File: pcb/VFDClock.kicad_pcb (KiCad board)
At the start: 4 copper layers, 80 x 52.7 mm, 84 parts, among them J1 Conn_01x04_Socket, J2 L_SIG_CONN, J3 L_PWR_CONN, J4 USB_C_Receptacle_USB2.0_16P, J5 R_SIG_CONN, J6 R_PWR_CONN, J7 Conn_02x06_Top_Bottom, Q1 BSS138, SW1 SW_SPST, SW2 SW_SPST, SW3 SW_SPST, SW4 SW_SPST, SW5 SW_SPST, SW6 SW_SPST, U1 TBD62783AFWG, U10 AMS1117-1.5, U2 ESP32-S3-WROOM-1, U3 IP4234CZ6, U4 TBD62783AFNG, U5 SN74HC595PWR, U6 AMS1117-3.3, U7 DS3231MZ+TRL, U8 SHT45-AD1B-R2, U9 VEML3235SL

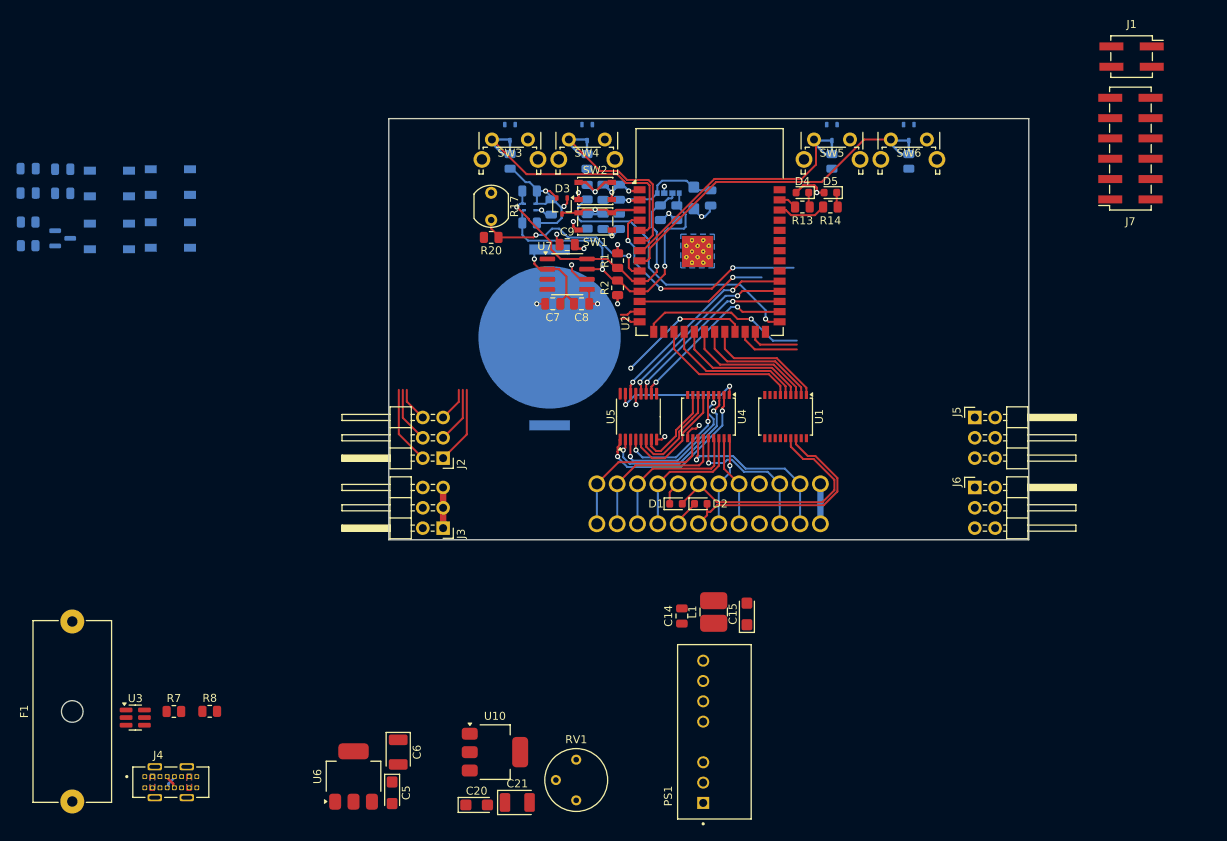
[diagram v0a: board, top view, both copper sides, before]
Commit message: Footprint placement done, PWR needs connecting
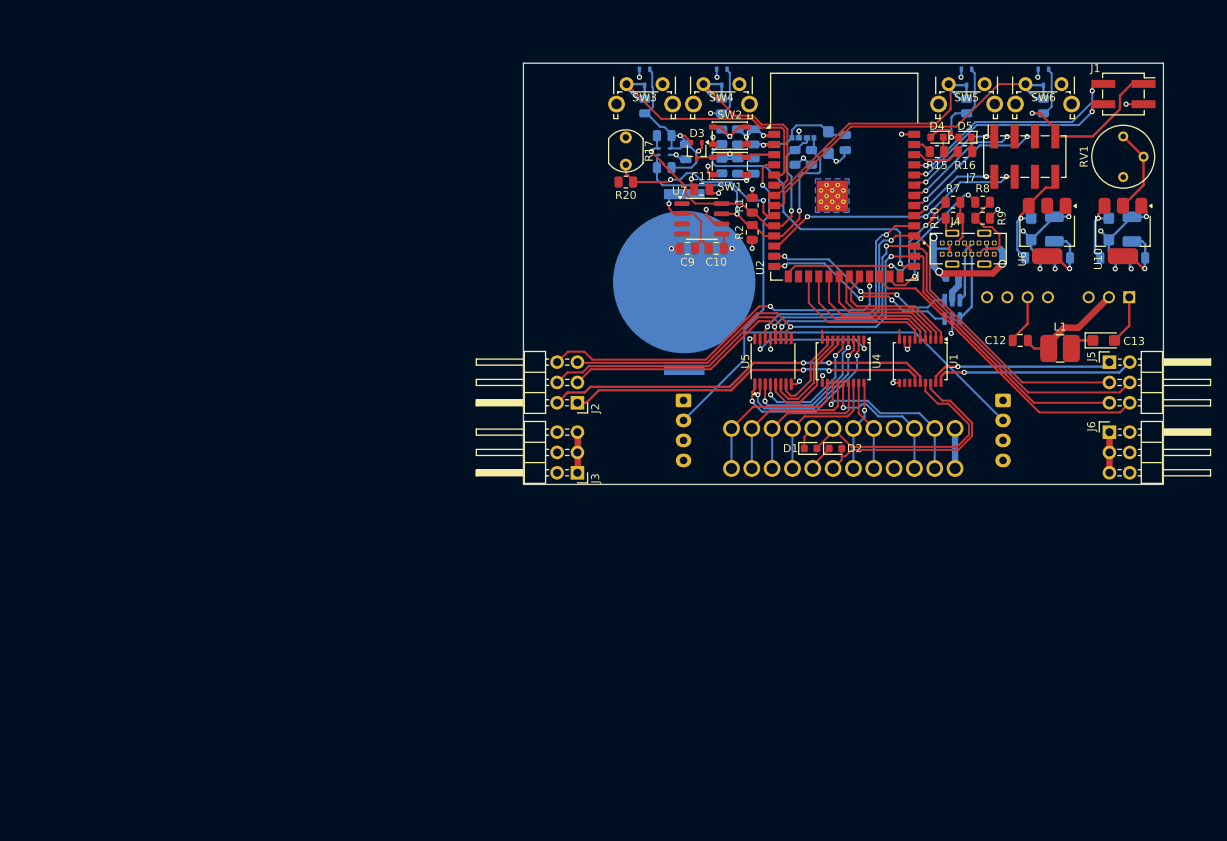
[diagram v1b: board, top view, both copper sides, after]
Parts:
- removed the C10 at (46.9, 95.7)
- removed the C11 at (46.9, 92.6)
- removed the C12 at (51.2, 95.7)
- removed the C13 at (51.2, 92.7)
- removed D10, D11: Inolux_IN-PI554FCH, LED_SMD:LED_Inolux_IN-PI554FCH_PLCC4_5.0x5.0mm_P3.2mm
- removed the D8 at (57.1, 101.1)
- removed the D9 at (57.1, 94.5)
- removed Q1: BSS138, Package_TO_SOT_SMD:SOT-23
- removed the R15 at (46.9, 102.2)
- removed the R16 at (46.9, 99.3)
- added C17: 100n, Capacitor_SMD:C_0805_2012Metric, B.Cu at (181.9, 103.8)
- added C20: 100n, Capacitor_SMD:C_0805_2012Metric, B.Cu at (185.6, 103.8)
- added C5: 100n, Capacitor_SMD:C_0805_2012Metric, B.Cu at (172.5, 103.8)
- added C8: 100n, Capacitor_SMD:C_0805_2012Metric, B.Cu at (176.2, 103.8)
- added J8: L_COL_CONN, Connector_JST:JST_XH_B4B-XH-A_1x04_P2.50mm_Vertical, B.Cu at (128.8, 121.6)
- added J9: R_COL_CONN, Connector_JST:JST_XH_B4B-XH-A_1x04_P2.50mm_Vertical, B.Cu at (168.8, 121.6)
- added R7: 100k, Resistor_SMD:R_0805_2012Metric, F.Cu at (162.5, 96.8)
- added R8: 100k, Resistor_SMD:R_0805_2012Metric, F.Cu at (166.2, 96.8)
- C18: renamed from C20; moved to B.Cu
- C19: renamed from C21; moved to B.Cu
- C6: renamed from C5; moved to B.Cu
- C7: renamed from C6; moved to B.Cu
- F1: value 3,5 A -> 2,5 A Fast Blow; footprint Fuse:Fuseholder_Cylinder-5x20mm_Schurter_0031_8201_Horizontal_Open -> Fuse:Fuse_0603_1608Metric; moved to B.Cu
- J7: value Conn_02x06_Top_Bottom -> CONN_GPIO; footprint Connector_PinSocket_2.54mm:PinSocket_2x06_P2.54mm_Vertical_SMD -> Connector_PinSocket_2.54mm:PinSocket_2x04_P2.54mm_Vertical_SMD
- PS1, U3: moved to B.Cu
- moved F1 128.0 mm to (162.4, 106.3), turned to 0 degrees
- moved J4 119.9 mm to (164.4, 102.6)
- moved R10 115.3 mm to (162.5, 98.8)
- moved R9 114.6 mm to (166.2, 98.8), turned to 180 degrees
- moved U3 114.2 mm to (162.4, 110.2), turned to 90 degrees
- moved U6 110.3 mm to (174.3, 100.4), turned to -90 degrees
- moved RV1 107.5 mm to (183.8, 88.6), turned to 180 degrees
- moved C18 106.9 mm to (182.0, 100.2), turned to -90 degrees
- moved C6 106.5 mm to (172.3, 100.2)
- moved C19 105.1 mm to (184.9, 100.2), turned to 90 degrees
- moved C7 104.9 mm to (175.2, 100.2), turned to 90 degrees
- moved U10 102.0 mm to (183.8, 100.4), turned to -90 degrees
- moved PS1 68.2 mm to (175.7, 110.1), turned to 180 degrees
- moved C13 56.2 mm to (181.4, 114.1), turned to 0 degrees
- moved C12 54.5 mm to (170.9, 114.1), turned to 180 degrees
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- renumbered C8 to C10, C9 to C11, C14 to C12, C15 to C13, C16 to C14, C17 to C15, C18 to C16, C7 to C9, D12 to D8, D13 to D9, R7 to R10, R9 to R11, R10 to R12, R11 to R13, R12 to R14, R13 to R15, R14 to R16, R8 to R9
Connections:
- F1 pad 1: +5V -> Net-(F1-Pad1)
- F1 pad 2: Net-(U3-VP) -> +5V
- J1 pad 3: Net-(J1-Pin_3) -> GND
- J1 pad 4: GND -> Net-(J1-Pin_4)
- J2 pad 2: /SRCLK -> /GRID_L2
- J2 pad 3: /GRID_L2 -> /RCLK
- J2 pad 4: //SRCLR -> /SRCLK
- J2 pad 5: /SER_LEFT -> //SRCLR
- J2 pad 6: /RCLK -> /SER_LEFT
- J4 pad A4: +5V -> Net-(F1-Pad1)
- J4 pad A9: +5V -> Net-(F1-Pad1)
- J4 pad B4: +5V -> Net-(F1-Pad1)
- J4 pad B9: +5V -> Net-(F1-Pad1)
- J5 pad 2: /SRCLK -> /GRID_R2
- J5 pad 3: /GRID_R2 -> /RCLK
- J5 pad 4: //SRCLR -> /SRCLK
- J5 pad 5: /SER_RIGHT -> //SRCLR
- J5 pad 6: /RCLK -> /SER_RIGHT
- J7 pad 1: +3V3 -> /GPIO42
- J7 pad 2: +5V -> /GPIO39
- J7 pad 3: /GPIO3 -> /GPIO41
- J7 pad 4: /GPIO41 -> /GPIO8
- J7 pad 5: /GPIO8 -> /GPIO40
- J7 pad 6: /GPIO42 -> GND
- J7 pad 7: /GPIO39 -> +3V3
- J7 pad 8: /GPIO48 -> +5V
- R10 pad 1: Net-(J4-CC1) -> GND
- R10 pad 2: GND -> Net-(J4-CC1)
- R9 pad 1: Net-(J4-CC2) -> GND
- R9 pad 2: GND -> Net-(J4-CC2)
- U2 pad 36: Net-(J1-Pin_3) -> Net-(J1-Pin_4)
- U3 pad 5: Net-(U3-VP) -> +5V
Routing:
- net /SRCLK: track 32.1 -> 96.7 mm
- net /RCLK: track 28.0 -> 91.7 mm
- net //SRCLR: track 28.3 -> 89.3 mm
- net +3V3: track 50.4 -> 111.2 mm, vias 8 -> 12
- net GND: track 37.2 -> 91.7 mm, vias 15 -> 33
- net /COLON_LED: track 29.1 -> 74.8 mm, vias 3 -> 1
- net /GRID_L2: track 7.02 -> 48.9 mm, vias 0 -> 2
- net /GRID_L1: track 9.77 -> 45.1 mm, vias 0 -> 2
- net +5V: track 5.08 -> 39.3 mm, vias 0 -> 2
- net /SER_RIGHT: track 7.95 -> 39.0 mm
- net Net-(J1-Pin_2): track 0.00 -> 29.2 mm, vias 0 -> 2
- net Net-(J1-Pin_4): track 0.00 -> 27.8 mm, vias 0 -> 2
- net /SER_LEFT: track 21.0 -> 46.7 mm
- net /GRID_R2: track 0.00 -> 25.1 mm, vias 0 -> 1
- net Net-(F1-Pad1): track 0.00 -> 24.2 mm, vias 0 -> 3
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- removed copper zone on B.Cu, net +5V
- removed copper zone on F.Cu, net +5V

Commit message: Layout done, generated fabrication files
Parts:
- added H1: MountingHole_Pad, MountingHole:MountingHole_3.2mm_M3_ISO14580_Pad_TopBottom, F.Cu at (112.2, 83.0)
- added H2: MountingHole_Pad, MountingHole:MountingHole_3.2mm_M3_ISO14580_Pad_TopBottom, F.Cu at (122.0, 128.0)
- added H3: MountingHole_Pad, MountingHole:MountingHole_3.2mm_M3_ISO14580_Pad_TopBottom, F.Cu at (176.0, 128.0)
- C1: value 22u -> 10u; footprint Capacitor_SMD:C_0805_2012Metric -> Capacitor_Tantalum_SMD:CP_EIA-3216-18_Kemet-A
- J2: value L_SIG_CONN -> R_SIG_CONN
- J5: value R_SIG_CONN -> L_SIG_CONN
- moved J8 39.9 mm to (168.8, 121.6)
- moved J9 39.9 mm to (128.8, 121.6)
- moved L1 2.98 mm to (175.9, 112.1)
- moved C13 2.59 mm to (179.7, 112.1), turned to -90 degrees
- moved C12 2.35 mm to (172.2, 112.1), turned to 90 degrees
- moved C1 0.63 mm to (135.6, 88.0)
- moved D3 0.18 mm to (130.3, 90.4)
- moved R12 0.08 mm to (133.5, 88.6)
- moved BT1 0.08 mm to (128.9, 106.7)
- moved C2 0.07 mm to (137.7, 88.6)
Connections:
- J2 pad 6: /SER_LEFT -> /SER_RIGHT
- J5 pad 6: /SER_RIGHT -> /SER_LEFT
- U2 pad 23: /SER_LEFT -> /SER_RIGHT
- U2 pad 24: /SER_RIGHT -> /SER_LEFT
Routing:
- net +3V3: track 111.2 -> 263.9 mm, vias 12 -> 14
- net +5V: track 39.3 -> 161.2 mm, vias 2 -> 8
- net Vfilament: track 5.00 -> 45.9 mm
- net Vbat: track 13.6 -> 43.0 mm, vias 1 -> 2
- net Vanode: track 8.54 -> 31.5 mm, vias 0 -> 2
- net Net-(F1-Pad1): track 24.2 -> 32.8 mm, vias 3 -> 2
- net /SER_RIGHT: track 39.0 -> 46.8 mm, vias 0 -> 2
- net /SER_LEFT: track 46.7 -> 39.0 mm, vias 2 -> 0
- net +1V5: track 19.0 -> 25.3 mm
- net GND: track 91.7 -> 95.1 mm, vias 33 -> 113
- net /SDA: track 41.5 -> 40.8 mm
- net Net-(U4-I1): track 16.5 -> 17.0 mm
- net /GPIO8: vias 3 -> 2
- added copper zone on B.Cu, net +5V
- added copper zone on In2.Cu, net +5V
- added copper zone on F.Cu, net Vanode
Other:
- board text added: "BOOT"
- board text added: "BTN1"
- board text added: "BTN2"
- board text added: "BTN3"
- board text added: "BTN4"
- board text added: "CR2032"
- board text added: "Filament ADJ"
- board text added: "L Module"
- board text added: "PWR"
- board text added: "R Module"
- board text added: "RST"
- board text added: "UART"

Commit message: Readded light sensor 3D model
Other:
- board text added: "PCB3D_BR_main"
- board text added: "PCB3D_TL_main"
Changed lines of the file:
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@@
 		)
 		(embedded_fonts no)
+		(model "${KIPRJMOD}/Models/VEML3235SL.stp"
+			(offset
+				(xyz 0 0.9 0.75)
+			)
+			(scale
+				(xyz 1 1 1)
+			)
+			(rotate
+				(xyz -90 -0 -0)
+			)
+		)
 	)
 	(footprint "Connector_PinSocket_2.54mm:PinSocket_1x12_P2.54mm_Vertical"
@@
 		)
 	)
+	(gr_text "PCB3D_TL_main"
+		(at 107.2 77.9 0)
+		(layer "Dwgs.User")
+		(effects
+			(font
+				(size 1 1)
+				(thickness 0.15)
+			)
+			(justify left bottom)
+		)
+	)
+	(gr_text "PCB3D_BR_main"
+		(at 190.8 134.6 0)
+		(layer "Dwgs.User")
+		(effects
+			(font
+				(size 1 1)
+				(thickness 0.15)
+			)
+			(justify left bottom)
+		)
+	)

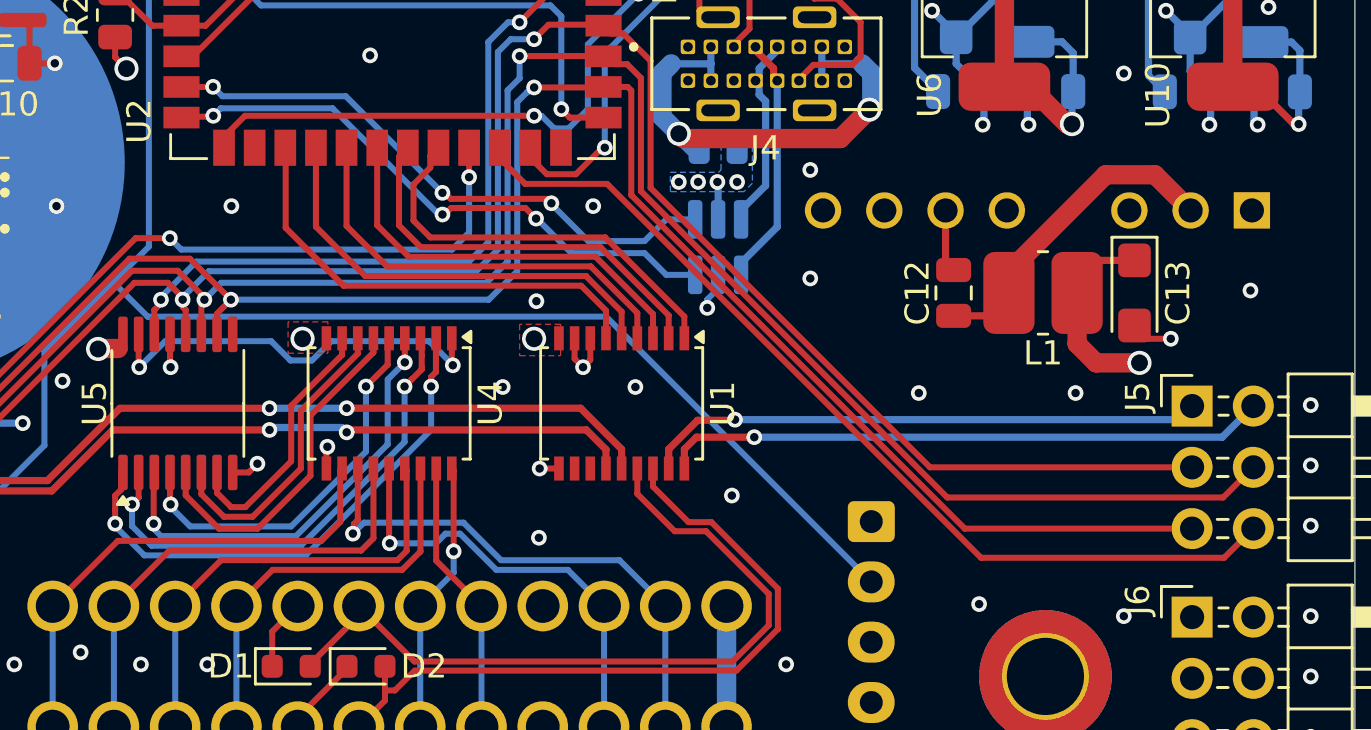
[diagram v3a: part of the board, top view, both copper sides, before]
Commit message: Modified circuit to use synchronous grid clock on all modules
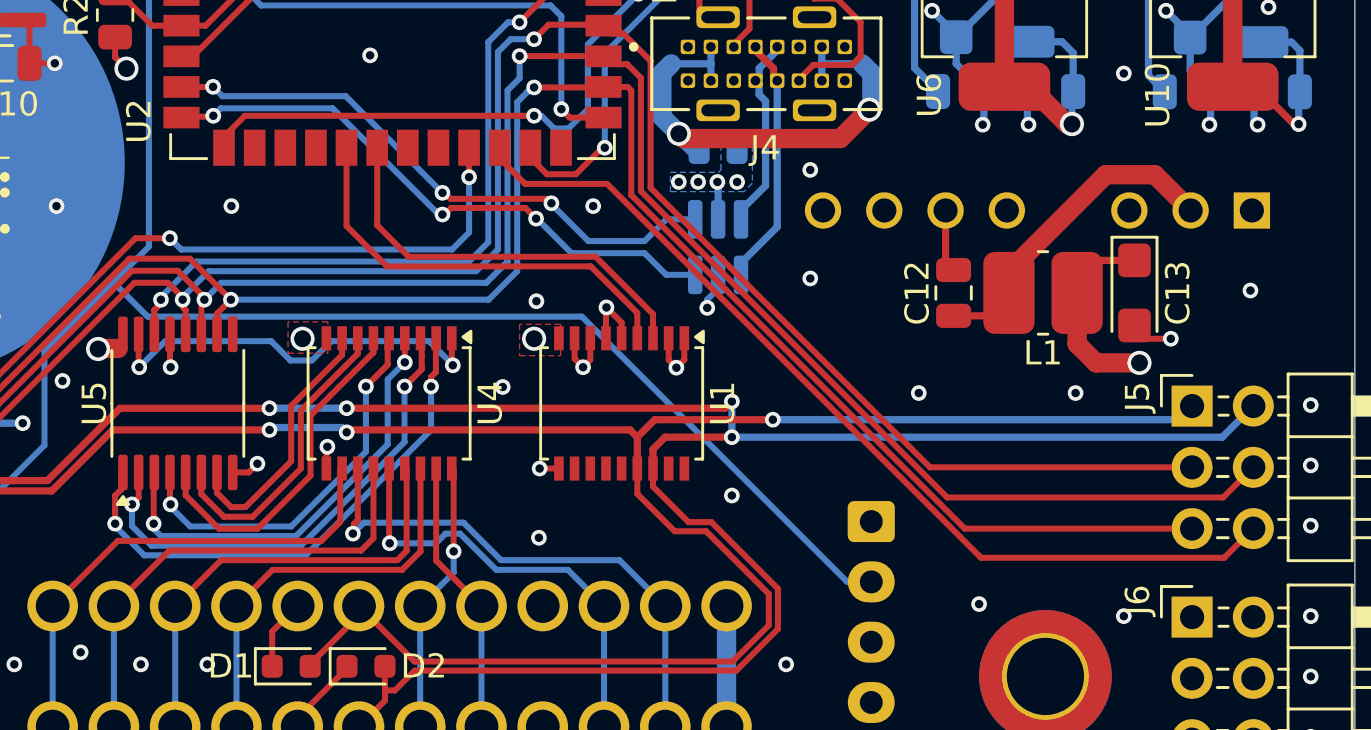
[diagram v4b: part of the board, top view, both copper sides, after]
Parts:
- J3: value L_PWR_CONN -> R_PWR_CONN
- J6: value R_PWR_CONN -> L_PWR_CONN
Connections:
- net /DRIVER_M1 renamed /DRIVER_1
- net /DRIVER_M2 renamed /DRIVER_2
- D1 pad 2: Net-(D1-A2) -> /GRID_1
- D2 pad 2: Net-(D2-A2) -> /GRID_2
- J2 pad 1: /GRID_L1 -> /GRID_1
- J2 pad 2: /GRID_L2 -> /GRID_2
- J5 pad 1: /GRID_R1 -> /GRID_1
- J5 pad 2: /GRID_R2 -> /GRID_2
- U1 pad 1: /DRIVER_R2 -> GND
- U1 pad 13: /GRID_L1 -> unconnected-(U1-O6-Pad13)
- U1 pad 14: /GRID_L2 -> unconnected-(U1-O5-Pad14)
- U1 pad 15: Net-(D1-A2) -> /GRID_1
- U1 pad 16: Net-(D2-A2) -> /GRID_2
- U1 pad 17: /GRID_R1 -> unconnected-(U1-O2-Pad17)
- U1 pad 18: /GRID_R2 -> unconnected-(U1-O1-Pad18)
- U1 pad 2: /DRIVER_R1 -> GND
- U1 pad 5: /DRIVER_L2 -> GND
- U1 pad 6: /DRIVER_L1 -> GND
- U2 pad 17: /DRIVER_L1 -> unconnected-(U2-IO9-Pad17)
- U2 pad 18: /DRIVER_L2 -> unconnected-(U2-IO10-Pad18)
- U2 pad 21: /DRIVER_R1 -> unconnected-(U2-IO13-Pad21)
- U2 pad 22: /DRIVER_R2 -> unconnected-(U2-IO14-Pad22)
- VFD1 pad 6: Net-(D1-A2) -> /GRID_1
- VFD2 pad 6: Net-(D2-A2) -> /GRID_2
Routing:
- net /GRID_2: track 0.00 -> 109.7 mm, vias 0 -> 4
- net /GRID_1: track 0.00 -> 101.8 mm, vias 0 -> 3
- net /GRID_L2: track 48.9 -> 0.00 mm, vias 2 -> 0
- net /GRID_L1: track 45.2 -> 0.00 mm, vias 2 -> 0
- net Net-(D1-A2): track 31.4 -> 0.00 mm
- net Net-(D2-A2): track 29.6 -> 0.00 mm
- net /GRID_R2: track 25.1 -> 0.00 mm, vias 1 -> 0
- net /GRID_R1: track 23.2 -> 0.00 mm, vias 1 -> 0
- net /DRIVER_L1: track 19.2 -> 0.00 mm
- net /DRIVER_L2: track 18.5 -> 0.00 mm
- net /DRIVER_R2: track 17.2 -> 0.00 mm
- net /DRIVER_R1: track 17.0 -> 0.00 mm
- net GND: track 95.1 -> 100.6 mm, vias 113 -> 114
- net +5V: track 161.2 -> 160.6 mm

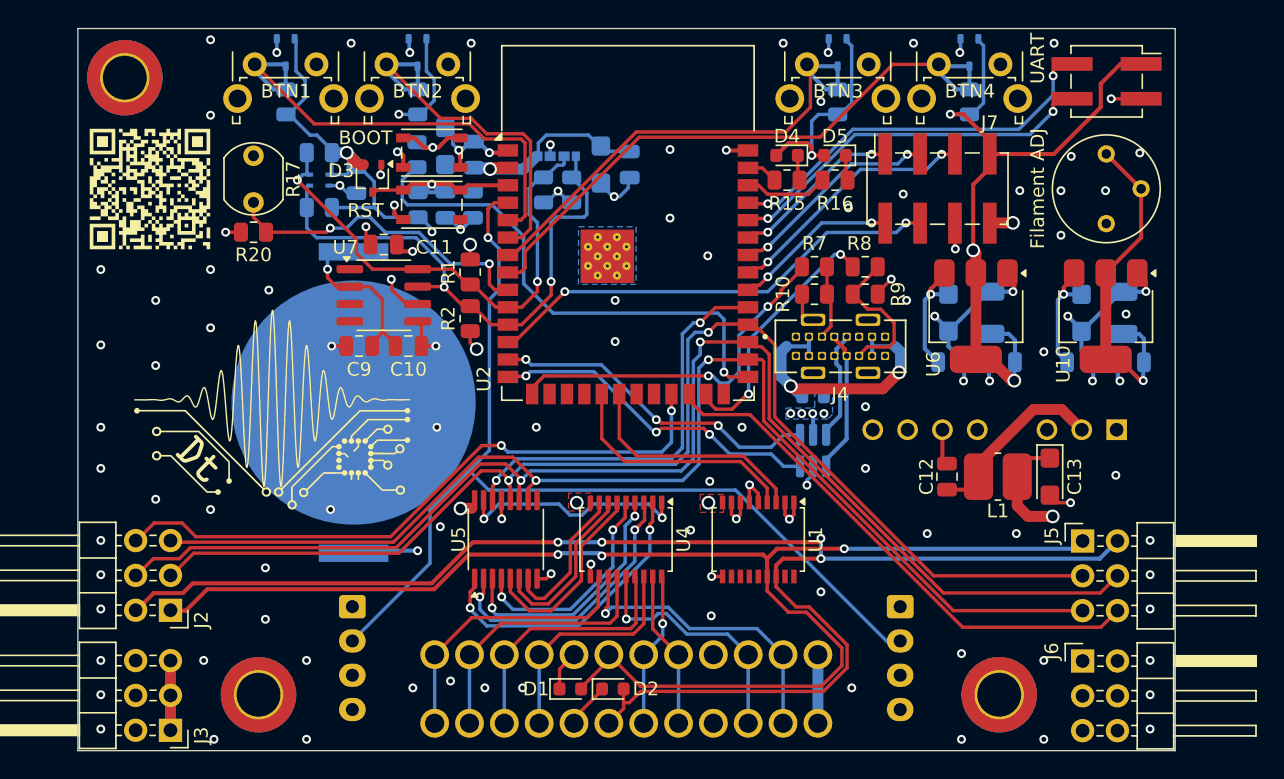
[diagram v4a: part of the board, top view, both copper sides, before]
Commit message: Fixed placement of mounting holes and pin headers
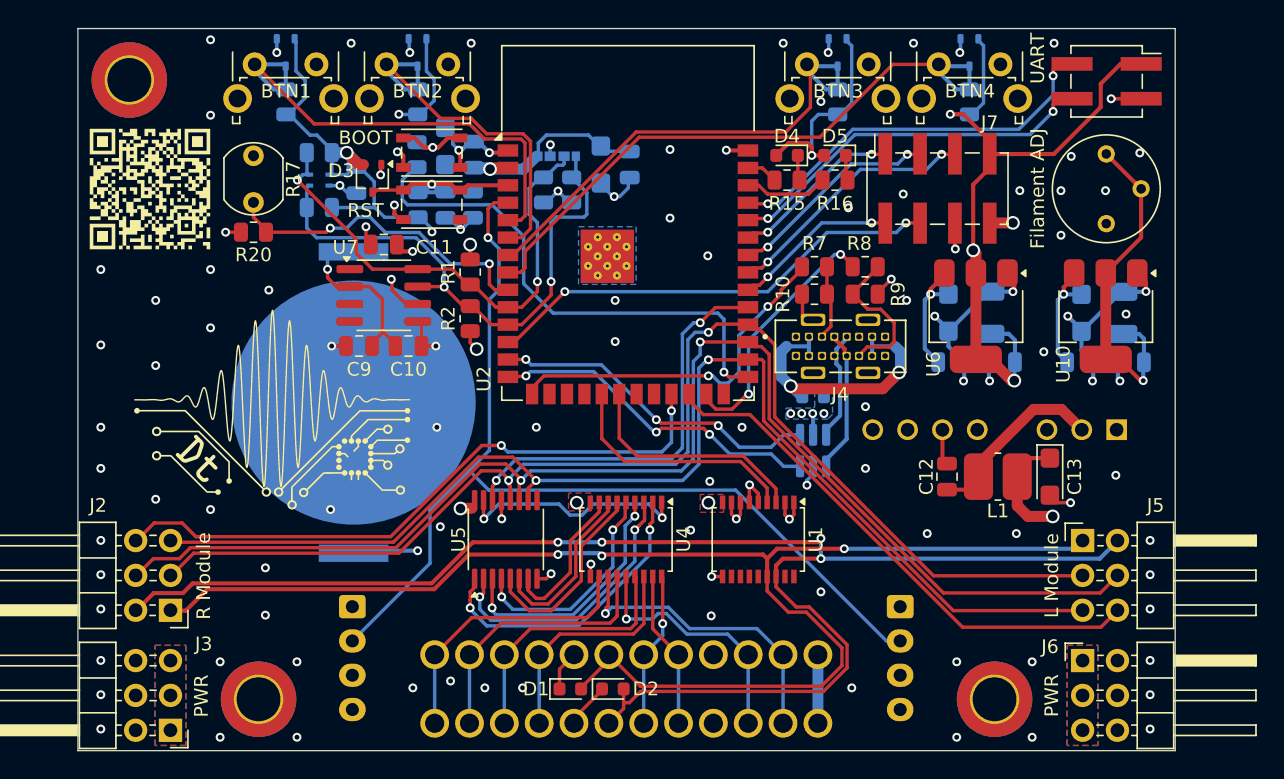
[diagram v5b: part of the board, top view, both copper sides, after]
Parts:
- moved H3 0.47 mm to (175.7, 128.3)
- moved H1 0.37 mm to (112.6, 83.2)
- moved H2 0.33 mm to (122.0, 128.3)
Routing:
- net +5V: track 160.6 -> 155.5 mm
- added copper zone on F.Cu, net +5V
- added copper zone on In1.Cu, net +5V
